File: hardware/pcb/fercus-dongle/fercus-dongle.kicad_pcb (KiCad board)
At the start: 2 copper layers, 11.5 x 16.4 mm, 20 parts, among them J1 USB_A, U1 CH32V208GBU6, U2 XC6206P332MR, Y1 32MHz, Y2 32.768kHz

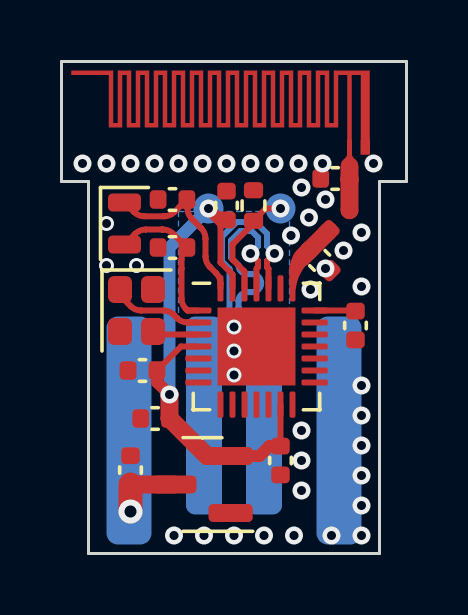
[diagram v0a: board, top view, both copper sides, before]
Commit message: merge
    fw:
    - fix usb product string, vid
    - add rf_phy_hop
    - add RF_BondingErase()
    - change default layout key fn to pause
    - fix power manager poweroff when usb disconnect
    - add usb compatibility interface

    hw:
    - change eta9084 iset resistor footprint to 0402
    - change fpc connector part
    - fix ir resistor value
    - change pcb thinkness to 1.6mm
    - fix footprint of pt and ir
    - fix rf ant trace
    - fix usb trace
    - add fercus-dongle-usb-c

    doc:
    - fix layout
    - add manual
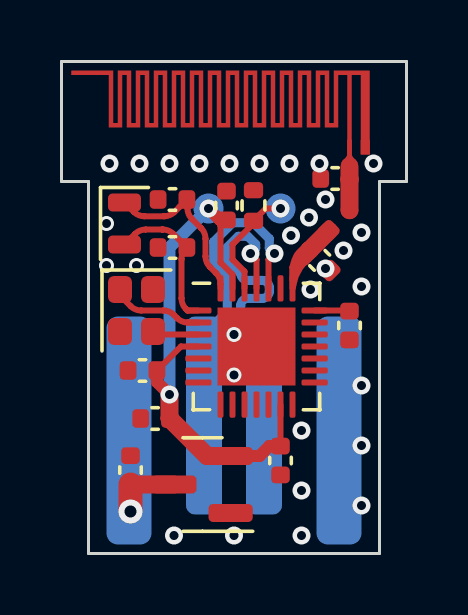
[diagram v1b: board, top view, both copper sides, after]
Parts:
- moved C4 0.20 mm to (29.6, 28.8)
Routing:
- net GND: vias 42 -> 30
